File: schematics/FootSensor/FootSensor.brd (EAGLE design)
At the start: 22.1 x 10.1 mm, 22 parts, among them IC1 MCP6V261, P1 PAD_THROUGH1, P2 PAD_THROUGH1, P3 PAD_THROUGH1, P4 PAD_THROUGH1, P5 PAD_THROUGH1, P6 PAD_THROUGH1, P7 PAD_THROUGH1, P8 PAD_THROUGH1, P9 PAD_THROUGH1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

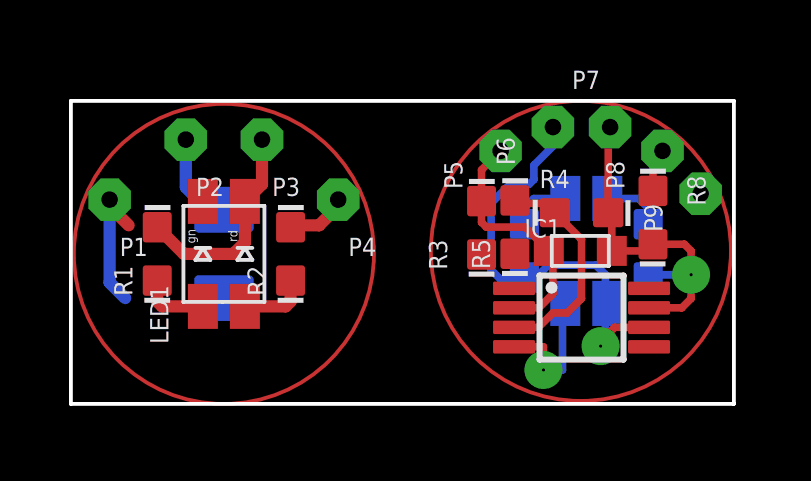
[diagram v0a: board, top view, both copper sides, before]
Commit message: Corrected silkscreen on Footsensor
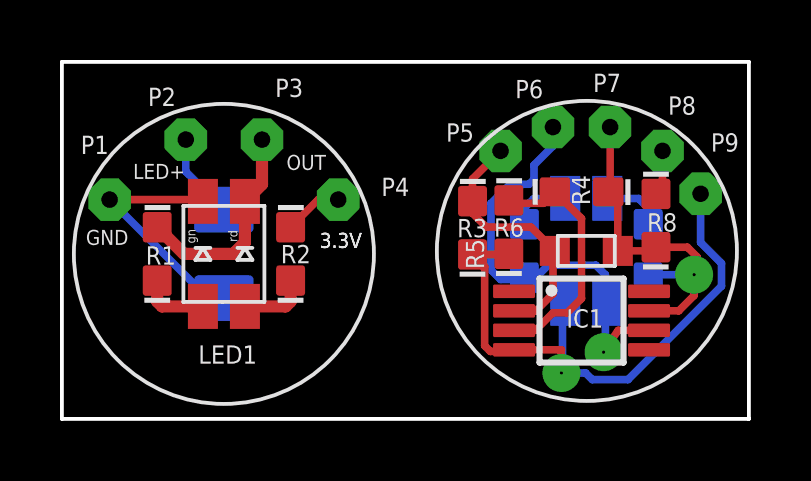
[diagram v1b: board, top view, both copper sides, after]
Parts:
- moved R4 0.70 mm to (-5.28, 2.67)
- moved R3 0.30 mm to (-8.91, 1.47)
- moved Q1 0.20 mm to (-5.12, 0.70)
- moved R5 0.20 mm to (-7.70, 1.49)
- moved R8 0.14 mm to (-2.80, 1.71)
- moved IC1 0.10 mm to (-5.28, -1.62)
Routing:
- net GND: track 9.26 -> 28.6 mm
- net N$1: track 7.43 -> 8.35 mm
- net LED+: track 4.37 -> 5.09 mm
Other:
- board size 22.1 x 10.1 mm -> 22.9 x 11.9 mm
- board text added: "3.3V"
- board text added: "GND"
- board text added: "LED+"
- board text added: "OUT"
- board text added: "SEN"

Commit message: Printed Toe, Foot & Thigh
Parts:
- R4: value S10K_0603 -> S51K_0603
- R5: value S20K_0603 -> S5.1K_0603
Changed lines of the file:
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@@
 </element>
 <element name="R6" library="joshi" package="0603R" value="S51R_0603" x="-7.18375" y="0.7" smashed="yes" rot="MR270">
-<attribute name="NAME" x="-8.197" y="1.17325" size="0.6096" layer="25" font="vector" ratio="12"/>
+<attribute name="NAME" x="-6.897" y="1.47325" size="0.6096" layer="26" font="vector" ratio="12"/>
 <attribute name="VALUE" x="-5.02475" y="2.097" size="0.6096" layer="28" font="vector" ratio="12" rot="MR270"/>
 </element>
@@
 <attribute name="VALUE" x="-0.8972625" y="2.097009375" size="0.6096" layer="28" font="vector" ratio="12" rot="MR270"/>
 </element>
-<element name="R4" library="joshi" package="0603R" value="S10K_0603" x="-5.27875" y="2.67" smashed="yes">
+<element name="R4" library="joshi" package="0603R" value="S51K_0603" x="-5.27875" y="2.67" smashed="yes">
 <attribute name="NAME" x="-4.9955" y="2.22425" size="0.6096" layer="25" font="vector" ratio="12" rot="R90"/>
 <attribute name="VALUE" x="-6.67575" y="1.146" size="0.6096" layer="27" font="vector" ratio="12"/>
 </element>
-<element name="R5" library="joshi" package="0603R" value="S20K_0603" x="-7.70125" y="1.49375" smashed="yes" rot="R90">
-<attribute name="NAME" x="-8.52675" y="0.09675" size="0.6096" layer="25" font="vector" ratio="12" rot="R90"/>
+<element name="R5" library="joshi" package="0603R" value="S5.1K_0603" x="-7.70125" y="1.49375" smashed="yes" rot="R90">
+<attribute name="NAME" x="-7.09675" y="1.77325" size="0.6096" layer="25" font="vector" ratio="12" rot="R180"/>
 <attribute name="VALUE" x="-6.17725" y="0.09675" size="0.6096" layer="27" font="vector" ratio="12" rot="R90"/>
 </element>
